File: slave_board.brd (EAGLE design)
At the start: 198.8 x 99.4 mm, 156 parts, among them IC3 ATMEGA2560-16AU, J11 1935161, J17 RJ45, J22 RJ45, J3 1935161, J6 1935161, K1 ORWH-SH-112D1F, Q1 PHB45NQ15T, Q2 PHB45NQ15T, Q3 BSS138L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

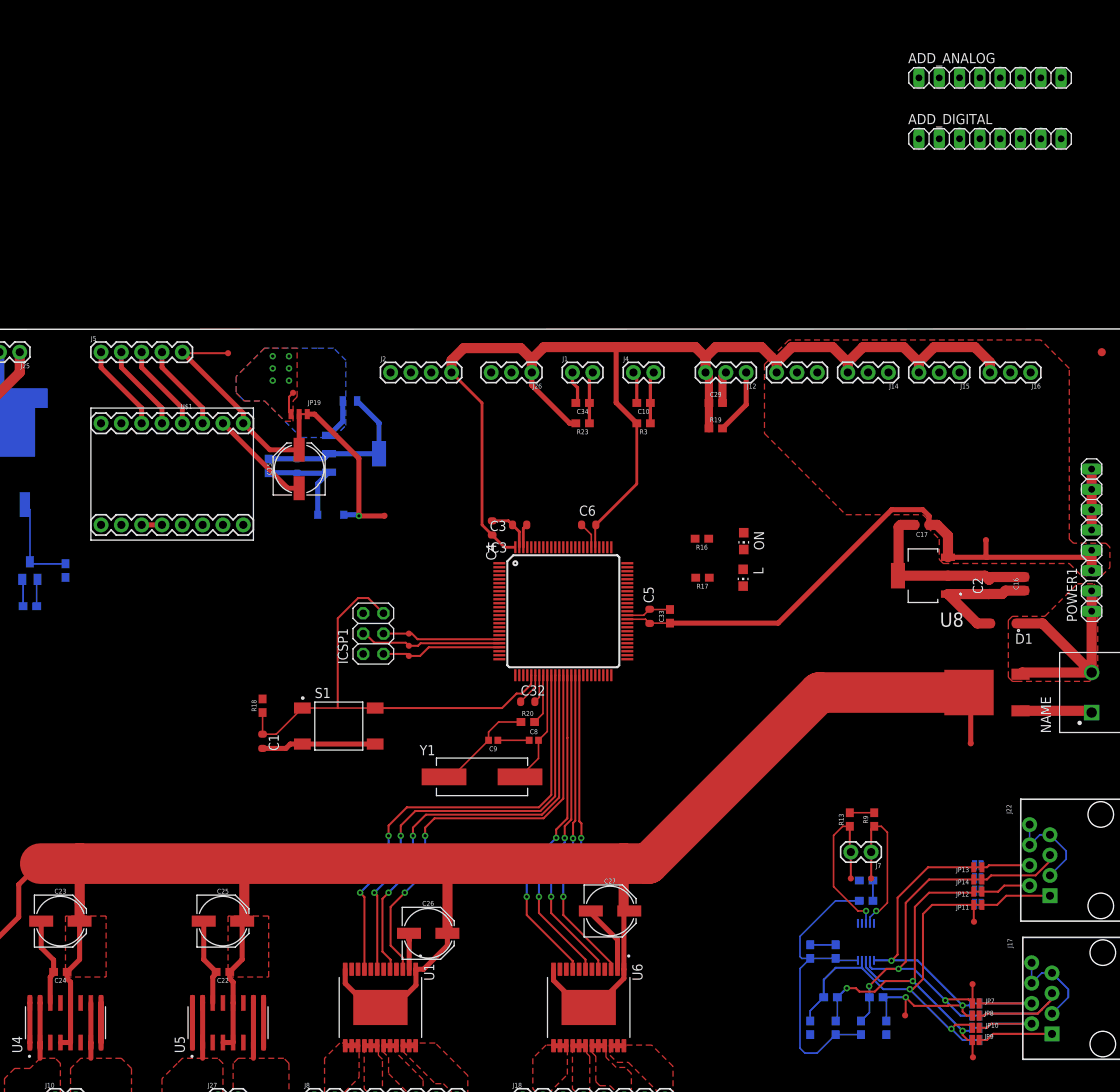
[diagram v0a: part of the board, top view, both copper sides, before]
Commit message: board progress - routing + ADC pin assignment
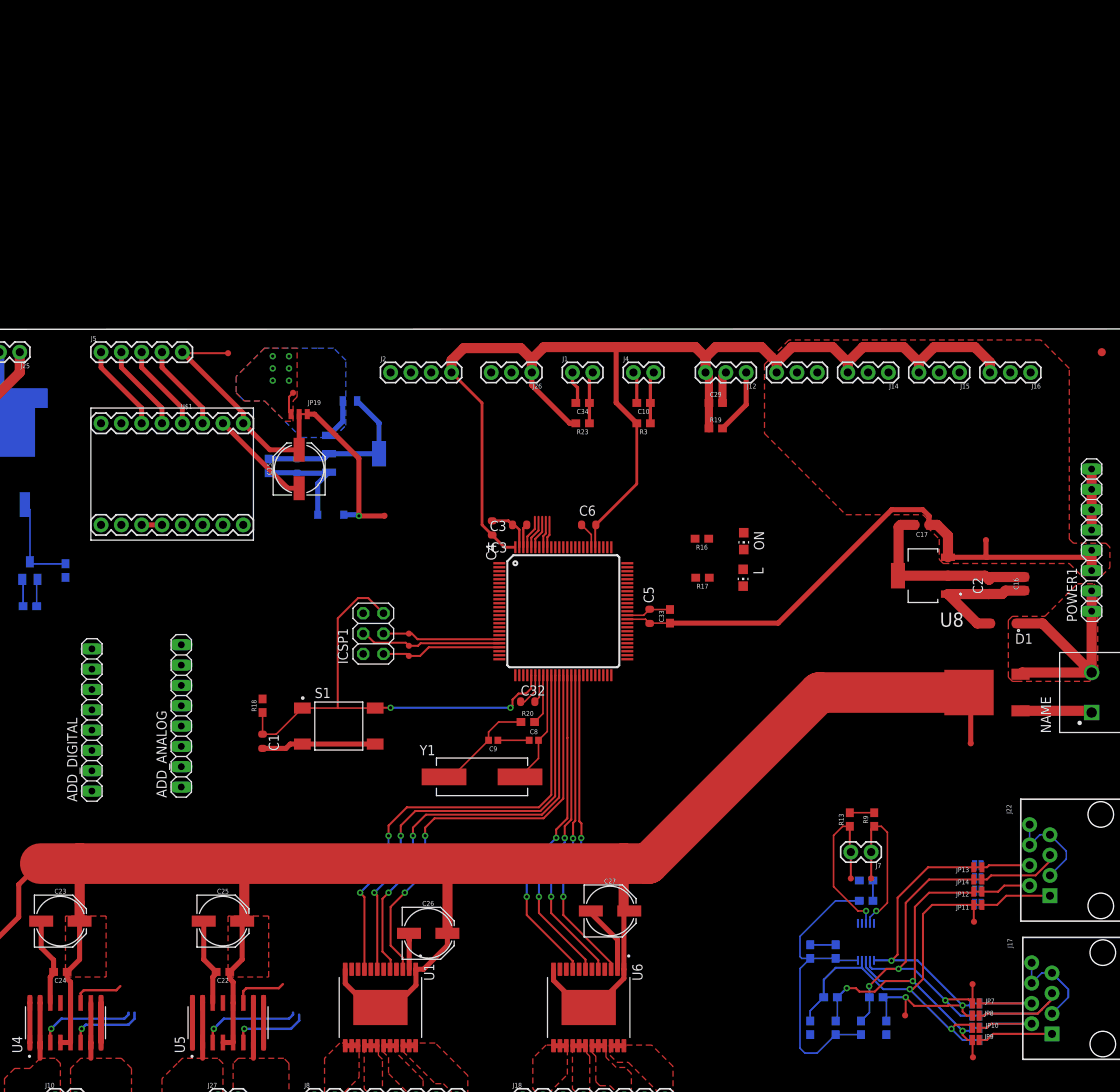
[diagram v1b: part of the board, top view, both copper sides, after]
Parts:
- moved ADD_DIGITAL 133.7 mm to (69.3, 50.5), turned to 90 degrees
- moved ADD_ANALOG 128.8 mm to (80.5, 51.1), turned to 90 degrees
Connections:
- net CAROUSEL_POS: now also IC3.95; no longer IC3.97
- net CUP_MASS0: now also IC3.93; no longer IC3.96
- net CUP_MASS1: now also IC3.92; no longer IC3.95
- net THERMISTOR0: now also IC3.97; no longer IC3.93
- net THERMISTOR1: now also IC3.96; no longer IC3.92
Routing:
- net ELEV_INA: track 0.00 -> 12.7 mm, vias 0 -> 1
- net PIVOT_INA: track 0.00 -> 12.4 mm, vias 0 -> 1
- net ELEV_INB: track 0.00 -> 9.81 mm, vias 0 -> 1
- net PIVOT_INB: track 0.00 -> 9.66 mm, vias 0 -> 1
- net ELEV_PWM: track 0.00 -> 6.78 mm
- net PIVOT_PWM: track 0.00 -> 6.53 mm
- net THERMISTOR0: track 6.52 -> 10.7 mm
- net THERMISTOR1: track 6.52 -> 10.7 mm
- net CAROUSEL_POS: track 8.21 -> 12.4 mm
- net CUP_MASS0: track 0.00 -> 3.94 mm
- net CUP_MASS1: track 0.00 -> 3.92 mm
- net RESET: track 59.1 -> 59.8 mm, vias 0 -> 2

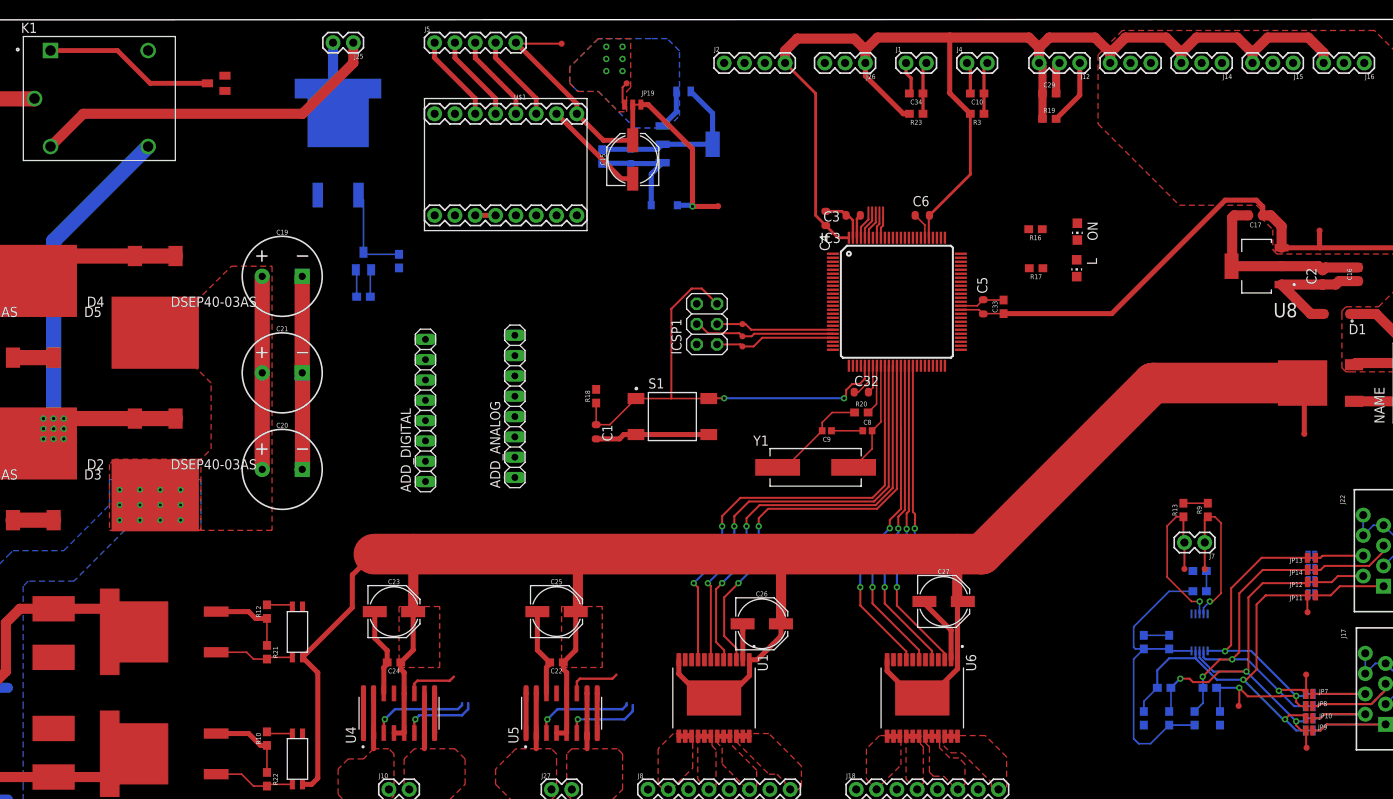
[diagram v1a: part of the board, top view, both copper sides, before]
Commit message: Routed mcu, except for additional pins
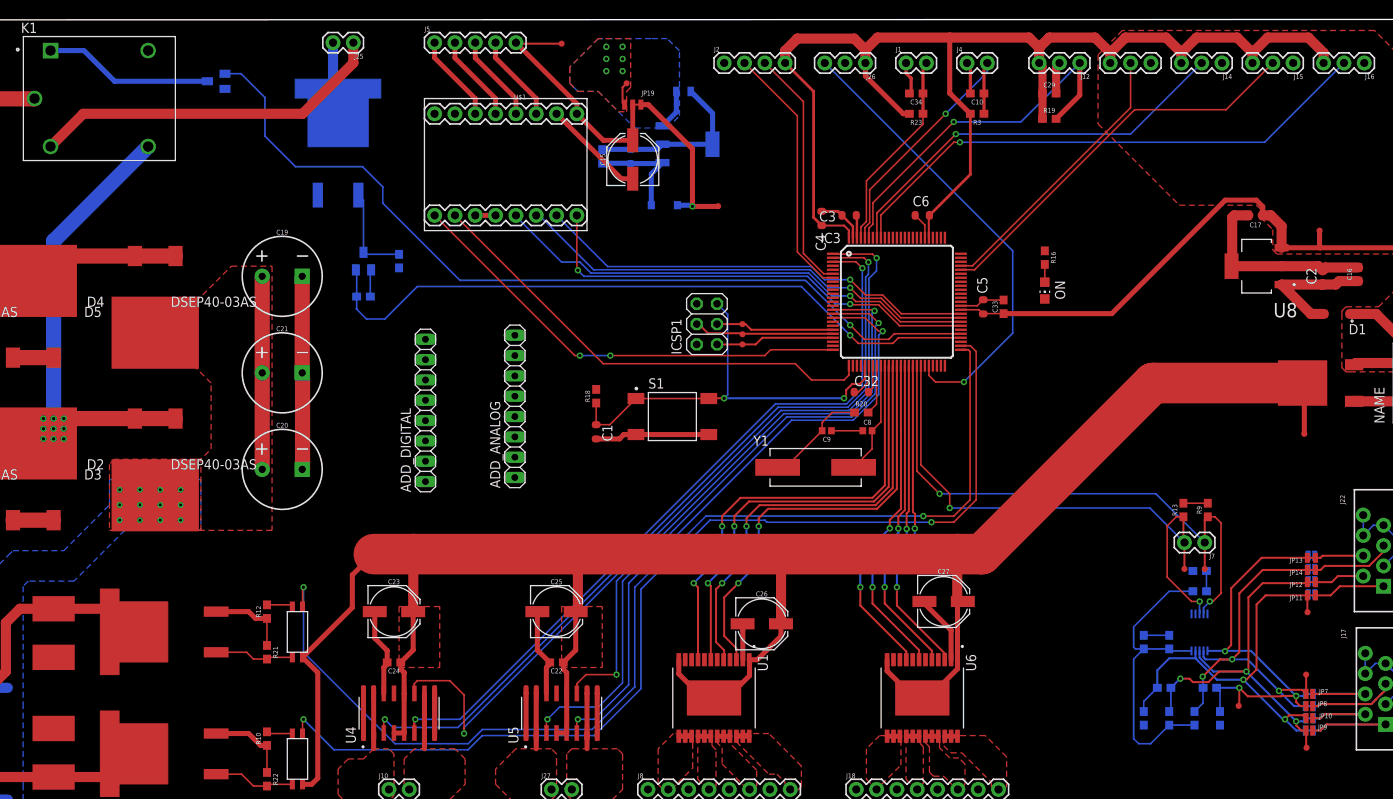
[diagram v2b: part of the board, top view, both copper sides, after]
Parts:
- removed L: YELLOW, led:CHIP-LED0805
- removed R17: 1k, SparkFun-Resistors:0603
- moved ON 8.41 mm to (146.8, 65.5)
- moved R16 3.74 mm to (146.8, 69.6), turned to 270 degrees
- moved C3 0.51 mm to (122.3, 74.9)
- moved C4 0.51 mm to (118.9, 74.5)
- moved Q5 0.25 mm to (43.2, 91.7), flipped to the bottom, turned to 270 degrees
- moved TP8 0.25 mm to (109.0, 58.8)
- moved TP7 0.25 mm to (109.0, 60.1)
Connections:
- removed net N$2: L.A, R17.2
- net CUP_SENSE0: now also IC3.72; no longer IC3.12
- net CUP_SENSE1: now also IC3.71; no longer IC3.13
- net GND: no longer L.C
- net STEP: no longer R17.1
- net THERMISTOR0: now also C34.1, J1.2, R23.1; no longer C10.1, J4.2, R3.1
- net THERMISTOR1: now also C10.1, J4.2, R3.1; no longer C34.1, J1.2, R23.1
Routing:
- net BLENDER0_EN: track 0.00 -> 138.3 mm, vias 0 -> 2
- net BLENDER1_EN: track 0.00 -> 128.7 mm, vias 0 -> 2
- net HEATPUMP_EN: track 0.00 -> 110.1 mm, vias 0 -> 1
- net PIVOT_PWM: track 6.53 -> 104.6 mm, vias 0 -> 2
- net PIVOT_INA: track 12.4 -> 100.5 mm, vias 1 -> 2
- net PIVOT_INB: track 9.66 -> 93.8 mm, vias 1 -> 2
- net COOLANT_EN: track 3.39 -> 85.9 mm, vias 0 -> 1
- net ELEV_INA: track 12.7 -> 82.2 mm, vias 1 -> 2
- net ELEV_INB: track 9.81 -> 78.7 mm, vias 1 -> 2
- net ELEV_PWM: track 6.78 -> 75.6 mm, vias 0 -> 2
- net CUP_MASS1: track 3.92 -> 68.6 mm, vias 0 -> 1
- net M2: track 0.00 -> 61.2 mm, vias 0 -> 1
- net STEP: track 0.00 -> 59.2 mm
- net M1: track 0.00 -> 58.4 mm, vias 0 -> 1
- net ELEV_ENC_OUT: track 0.00 -> 58.1 mm, vias 0 -> 1
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
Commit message: board progress - routing
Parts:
- added C35: 100n, SmartPrj:C0603-ROUND
- moved TP5 187.2 mm to (193.4, 92.8)
- moved TP3 157.5 mm to (173.4, 61.8)
- moved TP4 151.1 mm to (183.4, 20.4)
- moved TP6 124.7 mm to (103.1, 96.4)
- moved C1 15.5 mm to (106.2, 49.1)
- moved R18 14.5 mm to (105.2, 53.1)
- moved R16 4.61 mm to (144.3, 65.7), turned to 90 degrees
- moved TP2 4.49 mm to (102.6, 73.0)
- moved S1 2.29 mm to (97.9, 49.8)
- moved R15 2.17 mm to (65.3, 71.2), turned to 90 degrees
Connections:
- net +5V: now also C35.1; no longer C28.1, C7.1, Q3.G, R11.2, U$1./RESET, U$1./SLEEP, U3.3, U7.3
- net GND: now also C35.2
- net V-5_LOAD: now also C28.1, C7.1, Q3.G, R11.2, U$1./RESET, U$1./SLEEP, U3.3, U7.3
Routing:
- net GND: track 282.2 -> 476.7 mm, vias 0 -> 37
- net V-5_LOAD: track 8.00 -> 201.8 mm, vias 5 -> 9
- net +12V: track 96.9 -> 253.8 mm, vias 1 -> 20
- net +5V: track 289.0 -> 362.8 mm, vias 0 -> 4
- net CURR_SENS0: track 0.00 -> 58.5 mm
- net CURR_SENS1: track 0.00 -> 48.4 mm
- net V-HVDC: track 55.4 -> 95.9 mm
- net PIVOT_PWM: track 104.6 -> 98.5 mm
- net ELEV_ENC_OUT: track 58.1 -> 62.2 mm, vias 1 -> 2
- net RESET: track 53.6 -> 49.5 mm
- net CUP_SENSE1: vias 0 -> 1
- net CUP_SENSE0: vias 0 -> 1
- added copper zone on layer 16, net +12V
- added copper zone on layer 16, net GND

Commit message: board progress - power routing
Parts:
- moved ADD_DIGITAL 78.6 mm to (148.0, 51.2)
- moved TP14 6.03 mm to (172.0, 33.8)
- moved TP15 3.06 mm to (164.5, 33.8)
- moved J7 2.68 mm to (169.4, 33.8)
- moved R13 2.47 mm to (166.5, 37.6)
- moved R9 2.34 mm to (169.4, 37.6)
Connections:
- net CURR_SENS0: now also IC3.91
- net CURR_SENS1: now also IC3.90
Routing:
- net CURR_SENS1: track 48.4 -> 153.9 mm, vias 0 -> 4
- net CURR_SENS0: track 58.5 -> 161.0 mm, vias 0 -> 4
- net +5V: track 362.8 -> 452.8 mm, vias 4 -> 8
- net V-12V_PROT: track 276.2 -> 304.6 mm
- net SDA: track 72.4 -> 67.4 mm
- net SCL: track 74.0 -> 71.0 mm
- net ELEV_ENC_OUT: track 62.2 -> 61.4 mm
